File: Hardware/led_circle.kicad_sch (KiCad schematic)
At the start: 59 parts

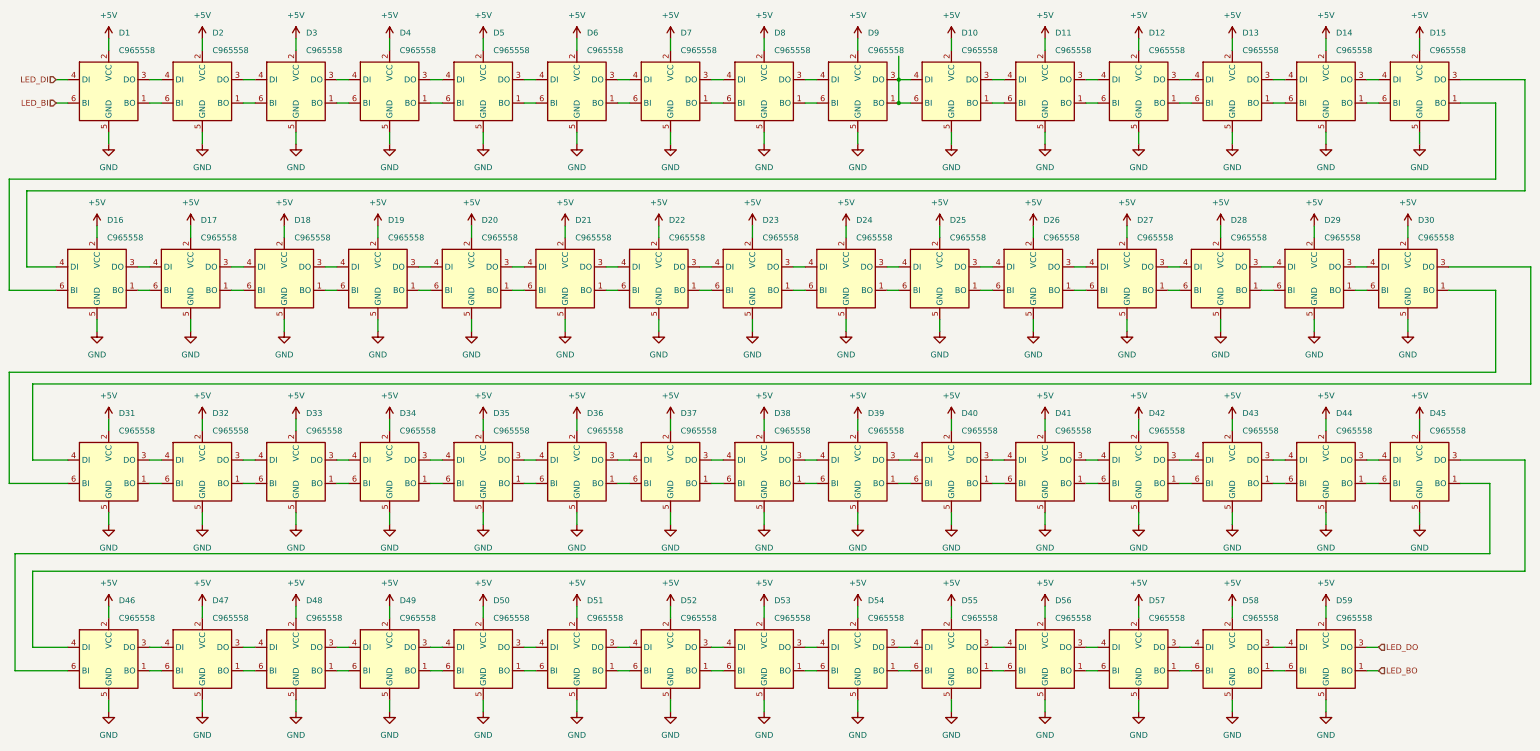
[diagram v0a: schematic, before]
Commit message: added LCSC number and datasheets
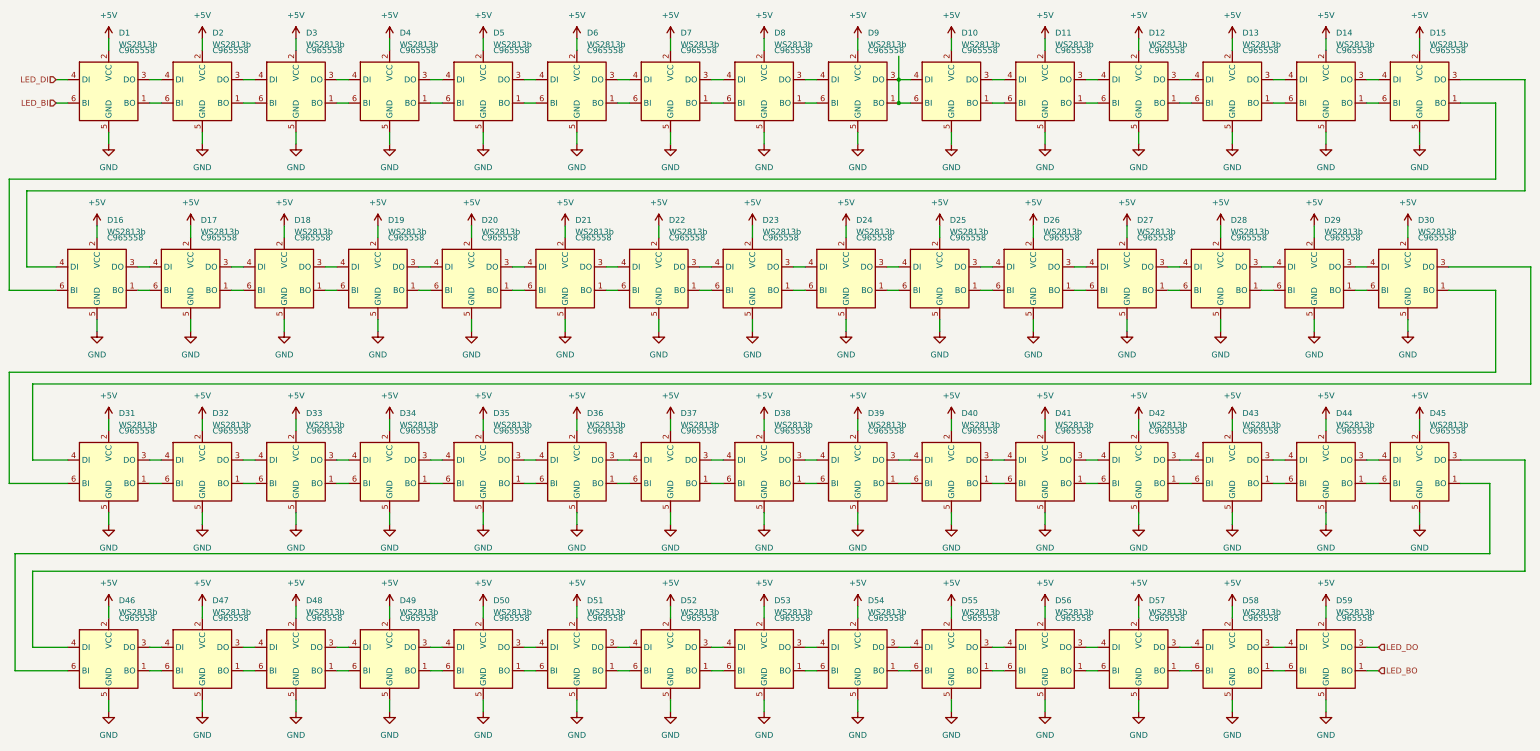
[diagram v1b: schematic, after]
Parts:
- D1, D10, D11, D12, D13, D14, D15, D16, D17, D18, D19, D2, D20, D21, D22, D23, D24, D25, D26, D27, D28, D29, D3, D30, D31, D32, D33, D34, D35, D36, D37, D38, D39, D4, D40, D41, D42, D43, D44, D45, D46, D47, D48, D49, D5, D50, D51, D52, D53, D54, D55, D56, D57, D58, D59, D6, D7, D8, D9: value ~ -> WS2813b
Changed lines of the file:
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@@
 			)
 		)
-		(property "Value" "~"
+		(property "Value" "WS2813b"
 			(at 160.9441 128.27 0)
 			(effects
@@
 			)
 		)
-		(property "Value" "~"
+		(property "Value" "WS2813b"
 			(at 320.9641 86.36 0)
 			(effects
@@
 			)
 		)
-		(property "Value" "~"
+		(property "Value" "WS2813b"
 			(at 262.5441 128.27 0)
 			(effects
@@
 			)
 		)
-		(property "Value" "~"
+		(property "Value" "WS2813b"
 			(at 120.3041 128.27 0)
 			(effects
@@
 			)
 		)
-		(property "Value" "~"
+		(property "Value" "WS2813b"
 			(at 59.3441 128.27 0)
 			(effects
@@
 			)
 		)
-		(property "Value" "~"
+		(property "Value" "WS2813b"
 			(at 77.1241 86.36 0)
 			(effects
@@
 			)
 		)
-		(property "Value" "~"
+		(property "Value" "WS2813b"
 			(at 138.0841 86.36 0)
 			(effects
@@
 			)
 		)
-		(property "Value" "~"
+		(property "Value" "WS2813b"
 			(at 56.8041 86.36 0)
 			(effects
@@
 			)
 		)
-		(property "Value" "~"
+		(property "Value" "WS2813b"
 			(at 79.6641 168.91 0)
 			(effects
@@
 			)
 		)
-		(property "Value" "~"
+		(property "Value" "WS2813b"
 			(at 341.2841 86.36 0)
 			(effects
@@
 			)
 		)
-		(property "Value" "~"
+		(property "Value" "WS2813b"
 			(at 181.2641 45.72 0)
 			(effects
@@
 			)
 		)
-		(property "Value" "~"
+		(property "Value" "WS2813b"
 			(at 140.6241 128.27 0)
 			(effects
@@
 			)
 		)
-		(property "Value" "~"
+		(property "Value" "WS2813b"
 			(at 120.3041 45.72 0)
 			(effects
@@
 			)
 		)
-		(property "Value" "~"
+		(property "Value" "WS2813b"
 			(at 99.9841 168.91 0)
 			(effects
@@
 			)
 		)
-		(property "Value" "~"
+		(property "Value" "WS2813b"
 			(at 300.6441 86.36 0)
 			(effects
@@
 			)
 		)
-		(property "Value" "~"
+		(property "Value" "WS2813b"
 			(at 97.4441 86.36 0)
 			(effects
@@
 			)
 		)
-		(property "Value" "~"
+		(property "Value" "WS2813b"
 			(at 181.2641 168.91 0)
 			(effects
@@
 			)
 		)
-		(property "Value" "~"
+		(property "Value" "WS2813b"
 			(at 178.7241 86.36 0)
 			(effects
@@
 			)
 		)
-		(property "Value" "~"
+		(property "Value" "WS2813b"
 			(at 343.8241 45.72 0)
 			(effects
@@
 			)
 		)
-		(property "Value" "~"
+		(property "Value" "WS2813b"
 			(at 59.3441 168.91 0)
 			(effects
@@
 			)
 		)
-		(property "Value" "~"
+		(property "Value" "WS2813b"
 			(at 201.5841 168.91 0)
 			(effects
@@
 			)
 		)
-		(property "Value" "~"
+		(property "Value" "WS2813b"
 			(at 117.7641 86.36 0)
 			(effects
@@
 			)
 		)
-		(property "Value" "~"
+		(property "Value" "WS2813b"
 			(at 280.3241 86.36 0)
 			(effects
@@
 			)
 		)
-		(property "Value" "~"
+		(property "Value" "WS2813b"
 			(at 158.4041 86.36 0)
 			(effects
@@
 			)
 		)
-		(property "Value" "~"
+		(property "Value" "WS2813b"
 			(at 201.5841 128.27 0)
 			(effects
@@
 			)
 		)
-		(property "Value" "~"
+		(property "Value" "WS2813b"
 			(at 201.5841 45.72 0)
 			(effects
@@
 			)
 		)
-		(property "Value" "~"
+		(property "Value" "WS2813b"
 			(at 140.6241 45.72 0)
 			(effects
@@
 			)
 		)
-		(property "Value" "~"
+		(property "Value" "WS2813b"
 			(at 99.9841 128.27 0)
 			(effects
@@
 			)
 		)
-		(property "Value" "~"
+		(property "Value" "WS2813b"
 			(at 181.2641 128.27 0)
 			(effects
@@
 			)
 		)
-		(property "Value" "~"
+		(property "Value" "WS2813b"
 			(at 221.9041 128.27 0)
 			(effects
@@
 			)
 		)
-		(property "Value" "~"
+		(property "Value" "WS2813b"
 			(at 260.0041 86.36 0)
 			(effects
@@
 			)
 		)
-		(property "Value" "~"
+		(property "Value" "WS2813b"
 			(at 242.2241 128.27 0)
 			(effects
@@
 			)
 		)
-		(property "Value" "~"
+		(property "Value" "WS2813b"
 			(at 221.9041 45.72 0)
 			(effects
@@
 			)
 		)
-		(property "Value" "~"
+		(property "Value" "WS2813b"
 			(at 160.9441 45.72 0)
 			(effects
@@
 			)
 		)
-		(property "Value" "~"
+		(property "Value" "WS2813b"
 			(at 262.5441 168.91 0)
 			(effects
@@
 			)
 		)
-		(property "Value" "~"
+		(property "Value" "WS2813b"
 			(at 79.6641 128.27 0)
 			(effects
@@
 			)
 		)
-		(property "Value" "~"
+		(property "Value" "WS2813b"
 			(at 140.6241 168.91 0)
 			(effects
@@
 			)
 		)
-		(property "Value" "~"
+		(property "Value" "WS2813b"
 			(at 242.2241 45.72 0)
 			(effects
@@
 			)
 		)
-		(property "Value" "~"
+		(property "Value" "WS2813b"
 			(at 59.3441 45.72 0)
 			(effects
@@
 			)
 		)
-		(property "Value" "~"
+		(property "Value" "WS2813b"
 			(at 282.8641 45.72 0)
 			(effects
@@
 			)
 		)
-		(property "Value" "~"
+		(property "Value" "WS2813b"
 			(at 282.8641 128.27 0)
 			(effects
@@
 			)
 		)
-		(property "Value" "~"
+		(property "Value" "WS2813b"
 			(at 99.9841 45.72 0)
 			(effects
@@
 			)
 		)
-		(property "Value" "~"
+		(property "Value" "WS2813b"
 			(at 323.5041 128.27 0)
 			(effects
@@
 			)
 		)
-		(property "Value" "~"
+		(property "Value" "WS2813b"
 			(at 221.9041 168.91 0)
 			(effects
@@
 			)
 		)
-		(property "Value" "~"
+		(property "Value" "WS2813b"
 			(at 199.0441 86.36 0)
 			(effects
@@
 			)
 		)
-		(property "Value" "~"
+		(property "Value" "WS2813b"
 			(at 303.1841 128.27 0)
 			(effects
@@
 			)
 		)
-		(property "Value" "~"
+		(property "Value" "WS2813b"
 			(at 303.1841 45.72 0)
 			(effects
@@
 			)
 		)
-		(property "Value" "~"
+		(property "Value" "WS2813b"
 			(at 303.1841 168.91 0)
 			(effects
@@
 			)
 		)
-		(property "Value" "~"
+		(property "Value" "WS2813b"
 			(at 343.8241 128.27 0)
 			(effects
@@
 			)
 		)
-		(property "Value" "~"
+		(property "Value" "WS2813b"
 			(at 323.5041 45.72 0)
 			(effects
@@
 			)
 		)
-		(property "Value" "~"
+		(property "Value" "WS2813b"
 			(at 262.5441 45.72 0)
 			(effects
@@
 			)
 		)
-		(property "Value" "~"
+		(property "Value" "WS2813b"
 			(at 242.2241 168.91 0)
 			(effects
@@
 			)
 		)
-		(property "Value" "~"
+		(property "Value" "WS2813b"
 			(at 120.3041 168.91 0)
 			(effects
@@
 			)
 		)
-		(property "Value" "~"
+		(property "Value" "WS2813b"
 			(at 323.5041 168.91 0)
 			(effects
@@
 			)
 		)
-		(property "Value" "~"
+		(property "Value" "WS2813b"
 			(at 282.8641 168.91 0)
 			(effects
@@
 			)
 		)
-		(property "Value" "~"
+		(property "Value" "WS2813b"
 			(at 79.6641 45.72 0)
 			(effects
@@
 			)
 		)
-		(property "Value" "~"
+		(property "Value" "WS2813b"
 			(at 239.6841 86.36 0)
 			(effects
@@
 			)
 		)
-		(property "Value" "~"
+		(property "Value" "WS2813b"
 			(at 219.3641 86.36 0)
 			(effects
@@
 			)
 		)
-		(property "Value" "~"
+		(property "Value" "WS2813b"
 			(at 160.9441 168.91 0)
 			(effects

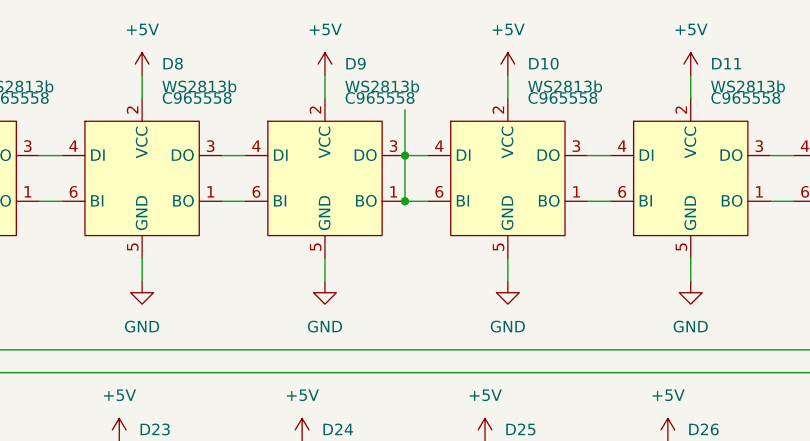
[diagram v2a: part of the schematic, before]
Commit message: impedance match 50R + 4 layer
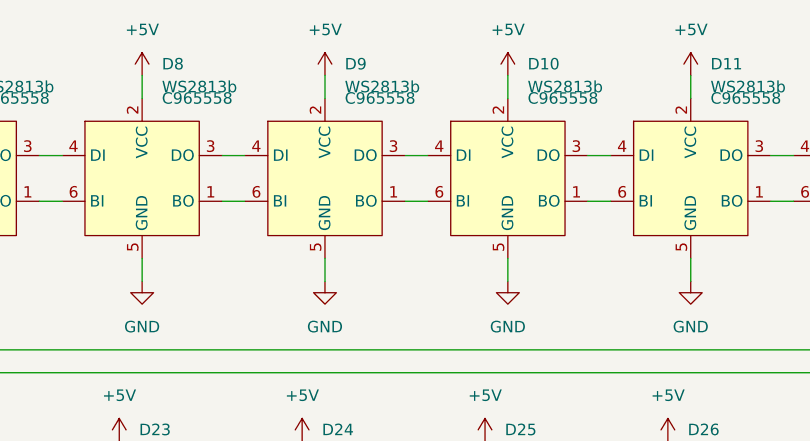
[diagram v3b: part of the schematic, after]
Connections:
- net at D10.6 (BI), D9.1 (BO): no longer D10.4 (DI), D9.3 (DO)
- new net: D10.4 (DI), D9.3 (DO)
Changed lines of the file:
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@@
 	(generator_version "8.0")
 	(paper "A3")
-	(junction
-		(at 228.6 53.34)
-		(diameter 0)
-		(color 0 0 0 0)
-	)
-	(junction
-		(at 228.6 58.42)
-		(diameter 0)
-		(color 0 0 0 0)
-	)
 	(wire
 		(pts
@@
 	(wire
 		(pts
-			(xy 228.6 58.42) (xy 228.6 53.34)
-		)
-		(stroke
-			(width 0)
-			(type default)
-		)
-	)
-	(wire
-		(pts
 			(xy 312.42 135.89) (xy 309.88 135.89)
 		)
@@
 		)
 		(stroke
-			(width 0)
-			(type default)
-		)
-	)
-	(wire
-		(pts
-			(xy 228.6 53.34) (xy 228.6 48.26)
-		)
-		(stroke
